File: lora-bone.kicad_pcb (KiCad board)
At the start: 2 copper layers, 30 x 100 mm, 28 parts, among them J1 Analog IN, J10 GS2, J11 GS2, J12 GS2, J13 GS2, J14 POWER OUT, J2 POWER, J3 Bluepill left, J4 PWM OUT, J5 SPI OUT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

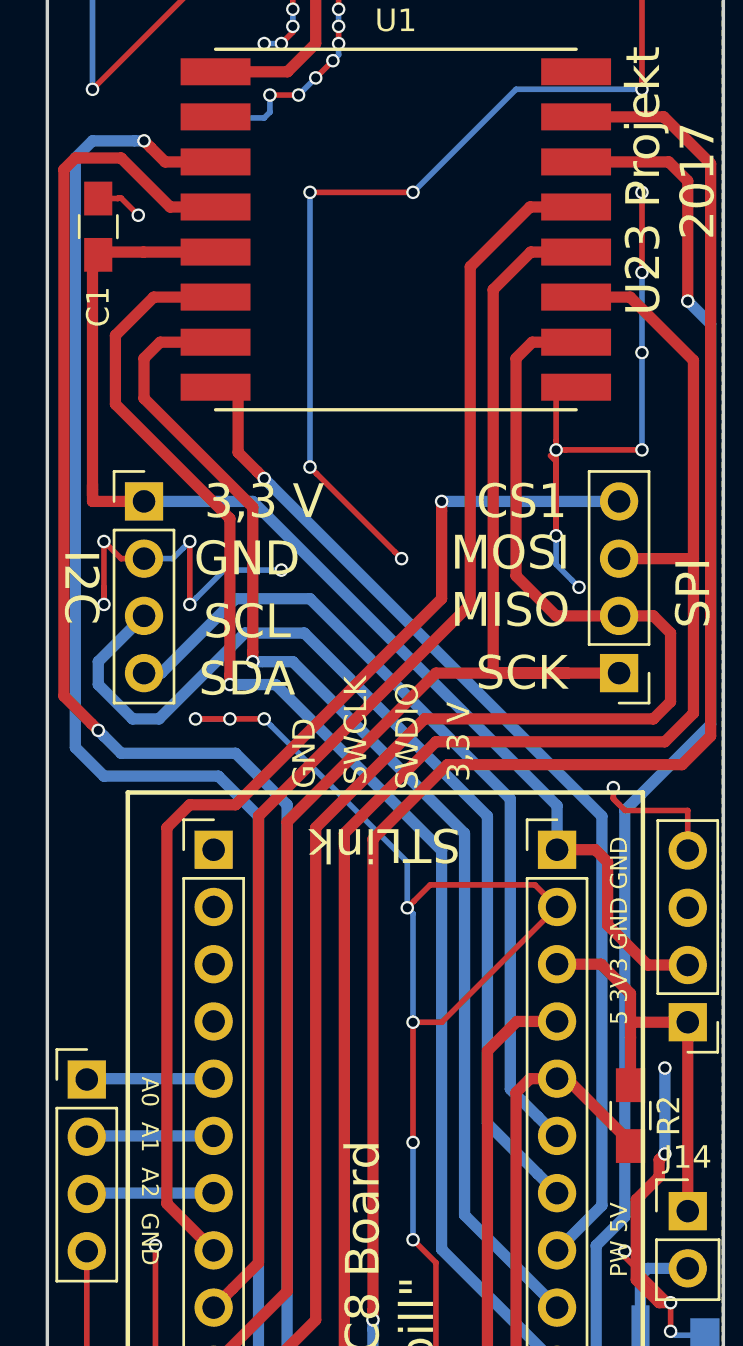
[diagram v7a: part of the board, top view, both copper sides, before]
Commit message: Added Pull Ups for I2C.
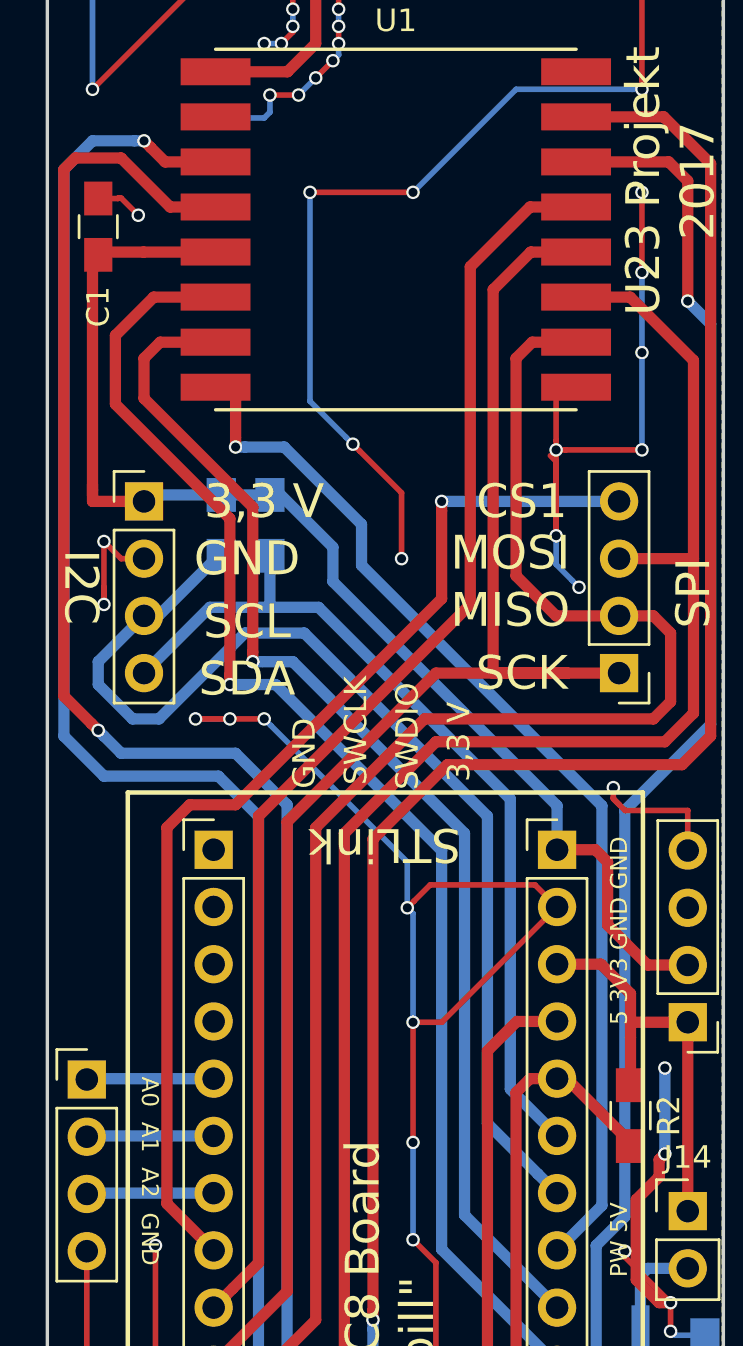
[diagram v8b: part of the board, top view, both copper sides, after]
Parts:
- added R3: 5k, Resistors_SMD:R_0805_HandSoldering, B.Cu at (37.7, 83.1)
- added R4: 5k, Resistors_SMD:R_0805_HandSoldering, B.Cu at (39.9, 83.1)
- moved G*** 2.79 mm to (45.6, 67.3)
- moved G*** 1.31 mm to (46.8, 90.2)
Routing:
- net GND: track 413.5 -> 403.6 mm, vias 73 -> 70
- net SCL: track 44.7 -> 49.3 mm
- net SDA: track 37.1 -> 39.1 mm
- net DIO2: track 45.8 -> 47.2 mm
- net +3V3: track 55.8 -> 56.9 mm
